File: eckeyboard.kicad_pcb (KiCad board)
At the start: 2 copper layers, 135.8 x 118.4 mm, 92 parts, among them J1 ICSP, J2 USB_B_Micro, J3 TRRS_Jack, J4 Conn_01x06_Male, J5 Conn_01x06_Male, J6 6P_ZH_connector, J7 6P_ZH_connector, SW1 RESET, U1 74HC4051, U2 NJM2742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

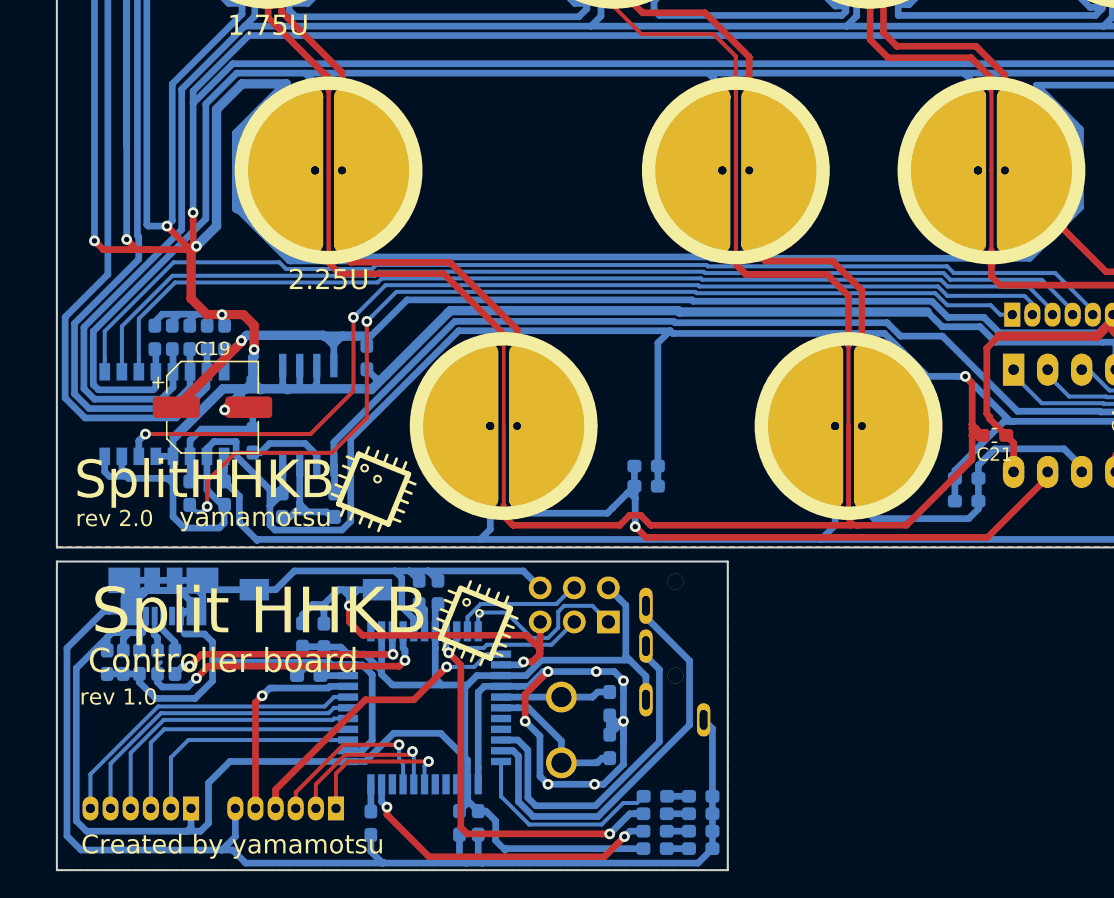
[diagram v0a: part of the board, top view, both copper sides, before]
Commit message: [remove] remove controller board
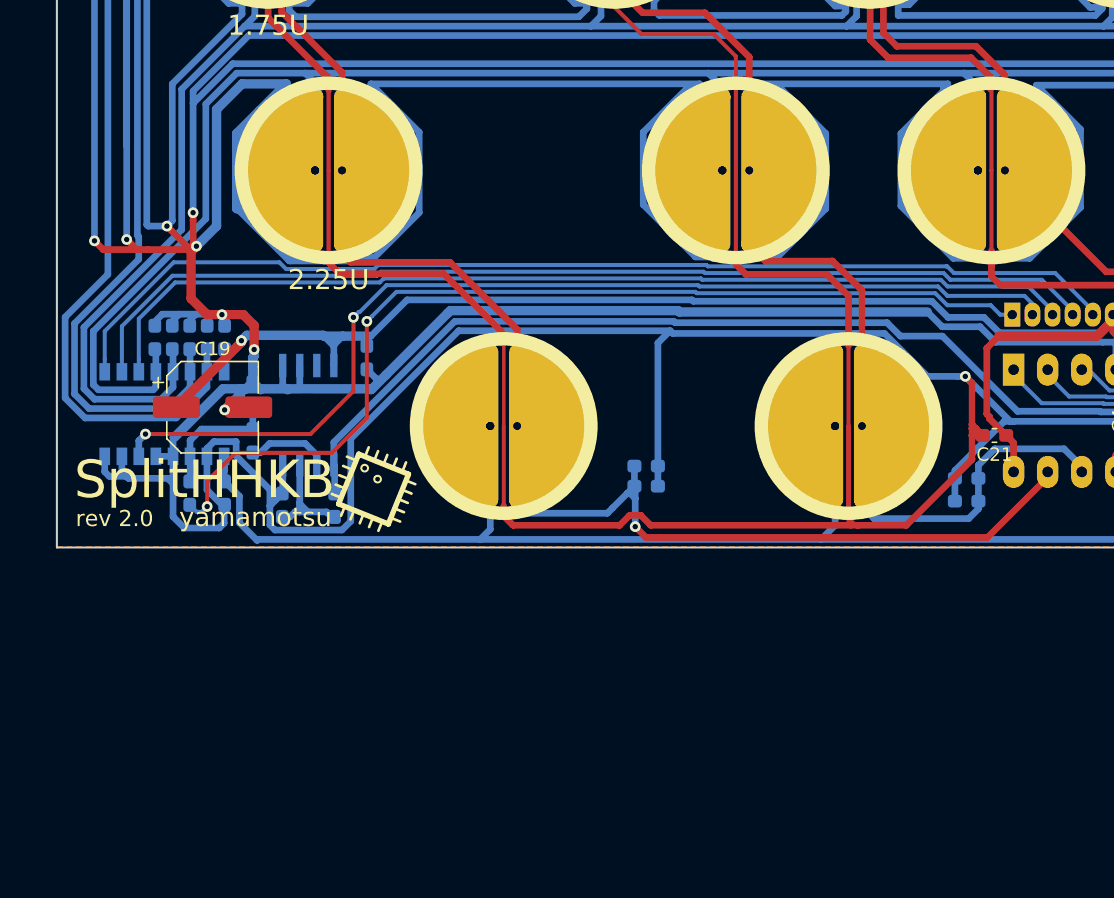
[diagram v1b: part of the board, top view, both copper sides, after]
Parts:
- removed C10: 100n, Capacitor_SMD:C_0603_1608Metric_Pad1.05x0.95mm_HandSolder
- removed C11, C15: 0.1u, Capacitor_SMD:C_0603_1608Metric_Pad1.05x0.95mm_HandSolder
- removed C12, C13, C14: 1u, Capacitor_SMD:C_0603_1608Metric_Pad1.05x0.95mm_HandSolder
- removed C16: 22u, Capacitor_SMD:C_0603_1608Metric_Pad1.05x0.95mm_HandSolder
- removed C8, C9: 22p, Capacitor_SMD:C_0603_1608Metric_Pad1.05x0.95mm_HandSolder
- removed D1: D, Diode_SMD:D_0603_1608Metric_Pad1.05x0.95mm_HandSolder
- removed D2: L, Diode_SMD:D_0603_1608Metric_Pad1.05x0.95mm_HandSolder
- removed D3: RX, Diode_SMD:D_0603_1608Metric_Pad1.05x0.95mm_HandSolder
- removed D4: TX, Diode_SMD:D_0603_1608Metric_Pad1.05x0.95mm_HandSolder
- removed D5: PWR, Diode_SMD:D_0603_1608Metric_Pad1.05x0.95mm_HandSolder
- removed J1: ICSP, Connector_PinHeader_2.54mm:PinHeader_2x03_P2.54mm_Vertical
- removed J2: USB_B_Micro, Connector_USB:USB_Micro-B_Molex_47346-0001
- removed J3: TRRS_Jack, MyLib:TRRS_jack_MJ4PP9
- removed J6, J7: 6P_ZH_connector, MyLib:ZH_6P_Horizontal
- removed R16, R21: 10k, Resistor_SMD:R_0603_1608Metric_Pad1.05x0.95mm_HandSolder
- removed R17, R18, R19, R20: 1k, Resistor_SMD:R_0603_1608Metric_Pad1.05x0.95mm_HandSolder
- removed R22, R23: 22, Resistor_SMD:R_0603_1608Metric_Pad1.05x0.95mm_HandSolder
- removed R24: 100k, Resistor_SMD:R_0603_1608Metric_Pad1.05x0.95mm_HandSolder
- removed the REF** at (72.2, 140.9)
- removed SW1: RESET, Button_Switch_SMD:SW_SPST_FSMSM
- removed U3: ATmega32U4-AU, Package_QFP:TQFP-44_10x10mm_P0.8mm
- removed Y1: 16MHz, Crystal:Crystal_HC50_Vertical
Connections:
- U2 pad 7: GND -> Net-(U2-Pad7)
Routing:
- net GND: track 3095.7 -> 2927.1 mm, vias 16 -> 9
- net +5V: track 243.1 -> 110.6 mm
- net /ArduinoLayer/RESET: track 33.4 -> 0.00 mm, vias 2 -> 0
- net /ArduinoLayer/Tx: track 31.1 -> 0.00 mm
- net /ArduinoLayer/RXLED: track 29.5 -> 0.00 mm, vias 2 -> 0
- net /ArduinoLayer/Rx: track 25.4 -> 0.00 mm
- net /ArduinoLayer/DRAIN: track 24.1 -> 0.00 mm
- net /ArduinoLayer/CLKLED: track 23.6 -> 0.00 mm, vias 2 -> 0
- net /ArduinoLayer/D-: track 23.2 -> 0.00 mm, vias 2 -> 0
- net /ArduinoLayer/MUX_EN: track 22.8 -> 0.00 mm
- net /ArduinoLayer/COL_EN: track 22.4 -> 0.00 mm, vias 1 -> 0
- net /ArduinoLayer/MUX_C: track 21.4 -> 0.00 mm
- net /ArduinoLayer/MUX_B: track 20.0 -> 0.00 mm
- net /ArduinoLayer/D+: track 18.6 -> 0.00 mm, vias 2 -> 0
- net /ArduinoLayer/MUX_A: track 17.5 -> 0.00 mm
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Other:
- board size 135.8 x 118.4 mm -> 135.8 x 94.3 mm
- board text removed: "A"
- board text removed: "B"
- board text removed: "C"
- board text removed: "COL_CONN"
- board text removed: "Controller board"
- board text removed: "Created by yamamotsu"
- board text removed: "DR"
- board text removed: "EN"
- board text removed: "GND"
- board text removed: "R"
- board text removed: "ROW_CONN"
- board text removed: "Split HHKB"
- board text removed: "VCC"
- board text removed: "rev 1.0"
